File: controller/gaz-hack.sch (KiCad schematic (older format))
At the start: 38 parts, among them K17 RELAY_SEPARATED, Q1 Q_NMOS_GSD, Q2 Q_NMOS_GSD, Q3 Q_PMOS_GSD, Q4 Q_NMOS_GSD, Q5 Q_PMOS_GSD, Q6 Q_PMOS_GSD, U1 OPTO-TRANSISTOR-4, U12 OPTO-TRANSISTOR-4, U4 OPTO-TRANSISTOR-4

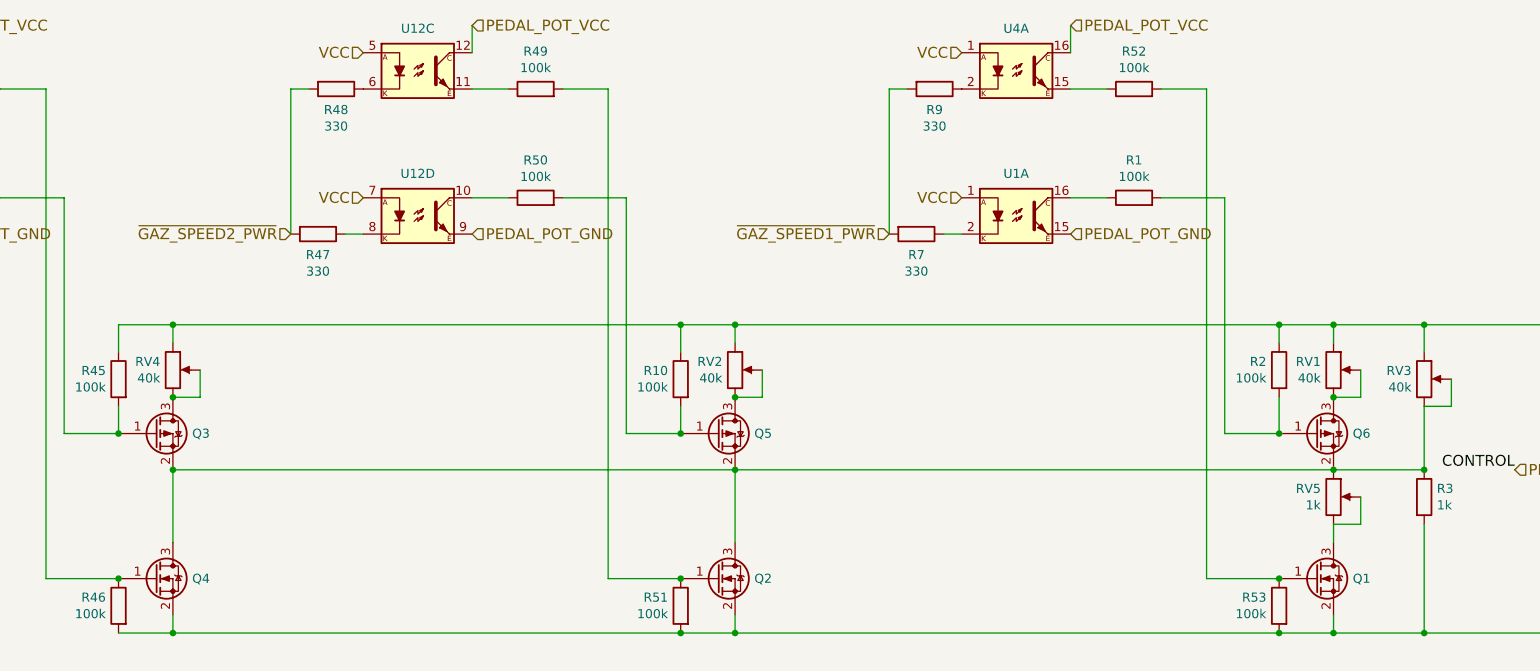
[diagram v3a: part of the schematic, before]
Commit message: Some progress with controller board routing
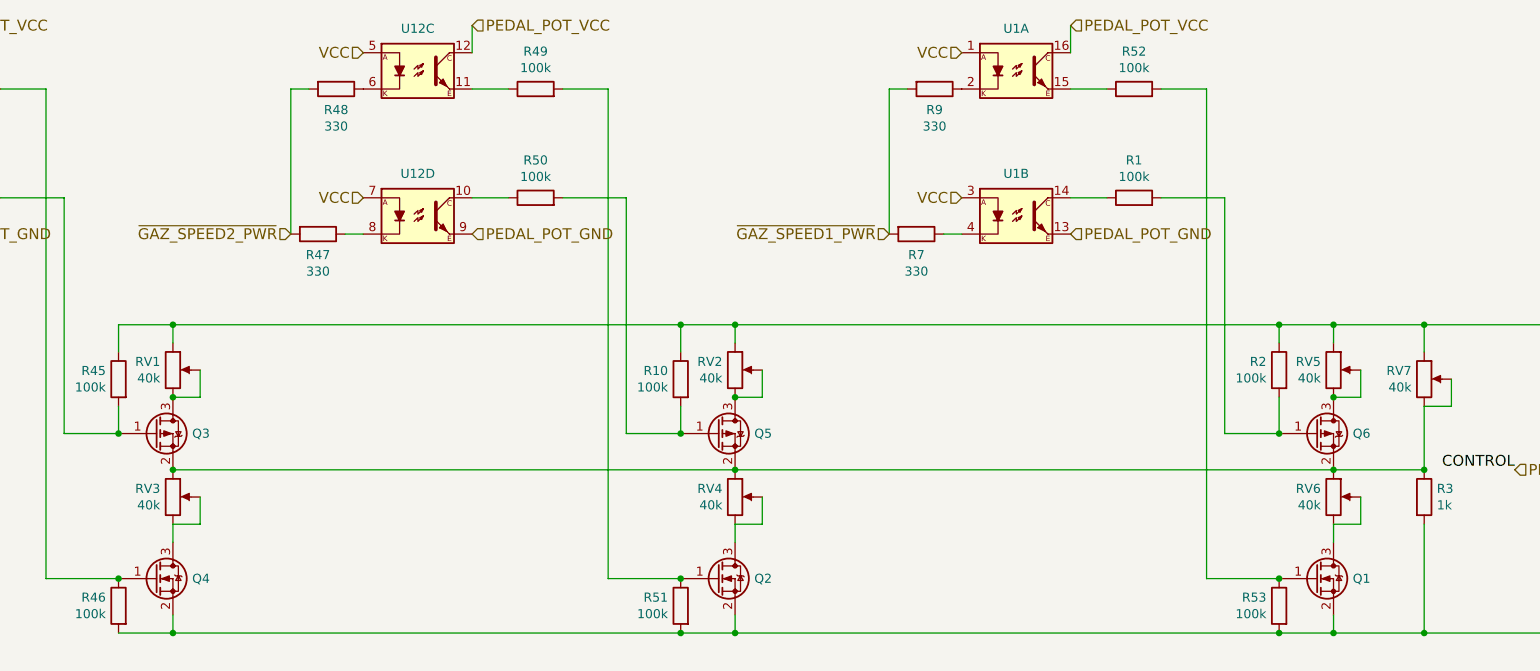
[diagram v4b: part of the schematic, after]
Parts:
- removed U4: OPTO-TRANSISTOR-4, symbol OPTO-TRANSISTOR-4
- added RV6, RV7: 40k, Potentiometers:Potentiometer_Trimmer_Bourns_3296P, symbol POT
- added unit 2 of U1
- Q1: Distributor (none) -> 2469640; Manufacturer (none) -> ?; PartNo (none) -> ?
- Q2, Q4: footprint Housings_SOT-23_SOT-143_TSOT-6:SOT-23_Handsoldering -> TO_SOT_Packages_SMD:SOT-23_Handsoldering; Distributor (none) -> 2469640; Manufacturer (none) -> ?; PartNo (none) -> ?
- Q3, Q5, Q6: footprint (none) -> TO_SOT_Packages_SMD:SOT-23_Handsoldering; Distributor (none) -> 1510765; Manufacturer (none) -> ?; PartNo (none) -> ?
- RV1, RV2, RV3, RV4: footprint (none) -> Potentiometers:Potentiometer_Trimmer_Bourns_3296P; Distributor (none) -> 9353135; Manufacturer (none) -> ?; PartNo (none) -> ?
- RV5: value 1k -> 40k; footprint (none) -> Potentiometers:Potentiometer_Trimmer_Bourns_3296P; Distributor (none) -> 9353135; Manufacturer (none) -> ?; PartNo (none) -> ?
- U1, U12: footprint (none) -> Housings_DIP:DIP-4_W11.48mm_SMD; Distributor (none) -> 1779744; Manufacturer (none) -> ?; PartNo (none) -> ?
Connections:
- net PEDAL_POT_GND: now also U1.13; no longer U1.15
- net PEDAL_POT_VCC: now also RV5.1, U1.16, RV7.1; no longer RV3.1, RV4.1
- net VCC: now also U1.3
- net at R1.1: now also U1.14; no longer U1.16
- net at R7.1: now also U1.4; no longer U1.2
- net at RV5.2, RV5.3: now also Q6.3 (D); no longer Q1.3 (D)
- net at RV1.2, RV1.3: now also Q3.3 (D); no longer Q6.3 (D)
- net at R52.1: now also U1.15
- net at R9.1: now also U1.2
- net at RV4.2, RV4.3: now also Q2.3 (D); no longer Q3.3 (D)
- new net: Q3.2 (S), Q5.2 (S), Q6.2 (S), R3.1, RV3.1, RV4.1, RV6.1, RV7.2, RV7.3
- new net: Q1.3 (D), RV6.2, RV6.3
- new net: Q4.3 (D), RV3.2, RV3.3

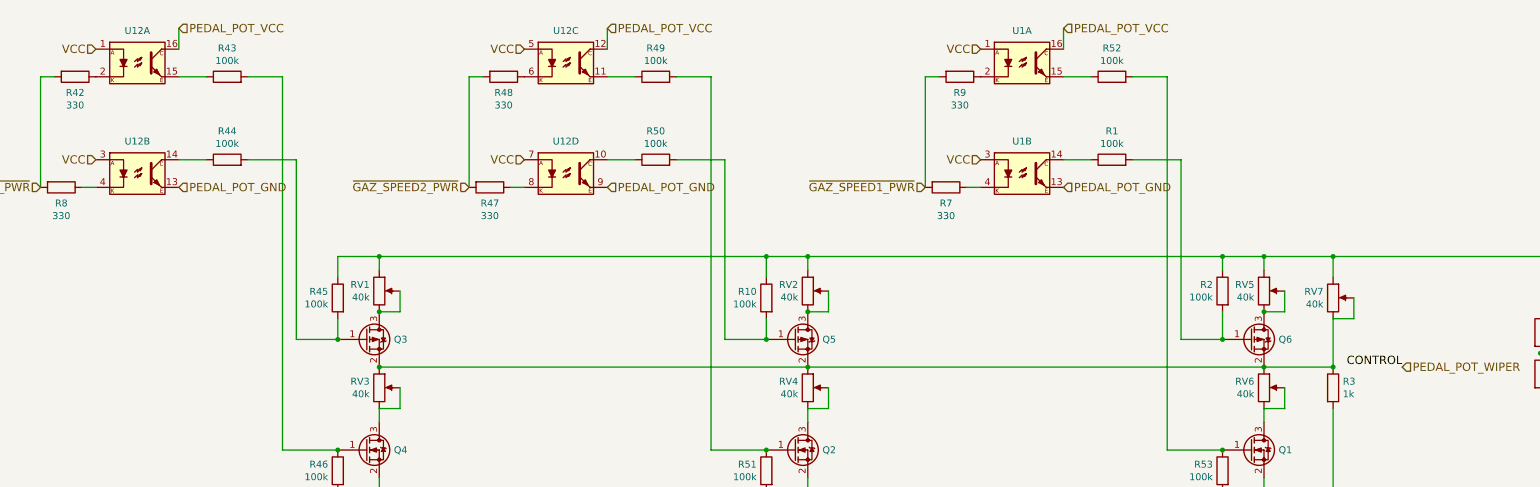
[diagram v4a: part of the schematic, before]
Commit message: Finish the routing, add some significant fixes: *correct to-252 pin numbering * longer pads for relays * fix footprint of the optocouplers
Also finish the routing
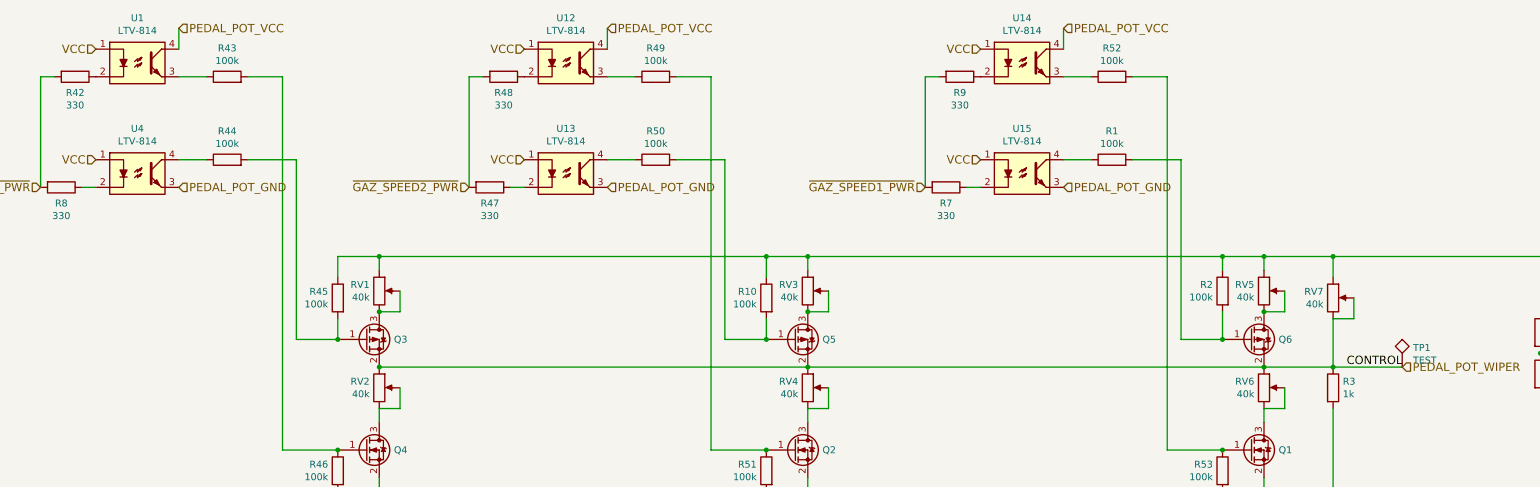
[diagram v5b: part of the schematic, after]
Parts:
- removed U1, U12: OPTO-TRANSISTOR-4, Housings_DIP:DIP-4_W11.48mm_SMD, symbol OPTO-TRANSISTOR-4
- added TP1: TEST, Measurement_Points:Measurement_Point_Round-TH_Small, symbol TEST
- added U1, U12, U13, U14, U15, U4: LTV-814, Housings_DIP:DIP-4_W11.48mm_SMD, symbol LTV-814
- RV1, RV2, RV3, RV4, RV5, RV6, RV7: footprint Potentiometers:Potentiometer_Trimmer_Bourns_3296P -> Potentiometers:Potentiometer_Trimmer_Bourns_3296W; Distributor 9353135 -> 9353305
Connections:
- net PEDAL_POT_GND: now also U13.3, U15.3, U4.3
- net PEDAL_POT_VCC: now also RV3.1, U1.4, U12.4, U14.4; no longer RV2.1
- net PEDAL_POT_WIPER: now also Q3.2 (S), Q5.2 (S), Q6.2 (S), R3.1, RV2.1, RV4.1, RV6.1, RV7.2, RV7.3, TP1.1
- net VCC: now also U1.1, U12.1, U13.1, U14.1, U15.1, U4.1
- net at R1.1: now also U15.4
- net at RV2.2, RV2.3: now also Q4.3 (D); no longer Q5.3 (D)
- net at R7.1: now also U15.2
- net at R9.1: now also U14.2
- net at RV3.2, RV3.3: now also Q5.3 (D); no longer Q4.3 (D)
- net at R52.1: now also U14.3
- net at R50.1: now also U13.4
- net at R47.1: now also U13.2
- net at R48.1: now also U12.2
- net at R49.1: now also U12.3
- net at R44.1: now also U4.4
- net at R43.1: now also U1.3
- net at R42.1: now also U1.2
- net at R8.1: now also U4.2

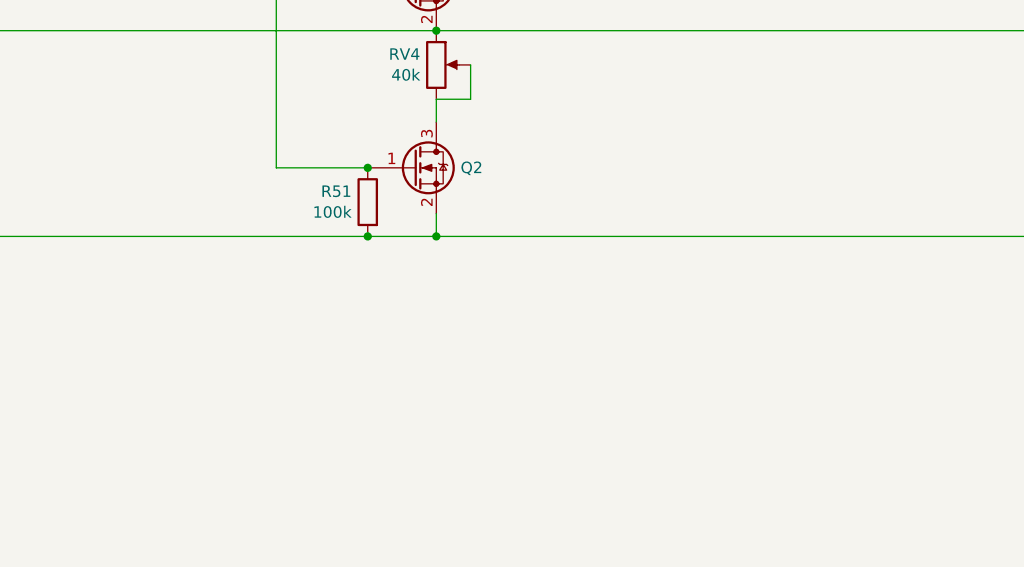
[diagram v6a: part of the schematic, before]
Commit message: add comments with fixes I had to make
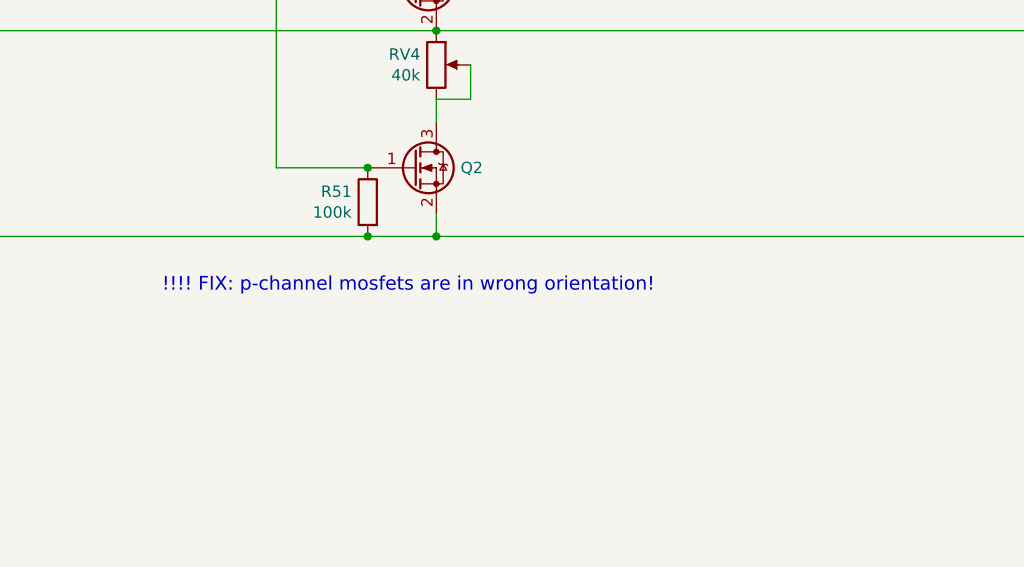
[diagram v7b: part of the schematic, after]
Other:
- note added: "!!!! FIX: p-channel mosfets are in wrong orientation!"
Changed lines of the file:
@@
 	1    0    0    -1
 $EndComp
+Text Notes 7350 6650 0    60   ~ 0
+!!!! FIX: p-channel mosfets are in wrong orientation!
 $EndSCHEMATC

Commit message: Last comments on the schematics
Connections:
- net PEDAL_POT_WIPER: now also Q6.3 (D); no longer Q6.2 (S)
- net at RV5.2, RV5.3: now also Q6.2 (S); no longer Q6.3 (D)
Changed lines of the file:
@@
 F 6 "1510765" H 11750 5300 60  0001 C CNN "Distributor"
 	1    11750 5300
-	1    0    0    -1
+	1    0    0    1
 $EndComp
 Wire Wire Line
